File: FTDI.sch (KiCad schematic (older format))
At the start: 4 parts, among them U2 FT232RL

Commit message: ready for check by another person
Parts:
- U2: footprint Button_Switch_SMD:SW_SPST_B3S-1000 -> Package_SO:SSOP-28_5.3x10.2mm_P0.65mm
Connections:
- net 3V3VOUT renamed 3V3VDD
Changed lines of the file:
@@
 AR Path="/5E190CFD" Ref="C?"  Part="1"
 AR Path="/5E18BB0B/5E190CFD" Ref="C12"  Part="1"
-AR Path="/5EBF9349/5E190CFD" Ref="C?"  Part="1"
-F 0 "C?" V 5900 1900 50  0000 L CNN
+AR Path="/5EBF9349/5E190CFD" Ref="C34"  Part="1"
+F 0 "C34" V 5900 1900 50  0000 L CNN
 F 1 "0.1uF" V 6000 1850 50  0000 L CNN
 F 2 "Capacitor_SMD:C_0603_1608Metric" H 6188 1800 50  0001 C CNN
@@
 AR Path="/5E190D03" Ref="U?"  Part="1"
 AR Path="/5E18BB0B/5E190D03" Ref="U2"  Part="1"
-AR Path="/5EBF9349/5E190D03" Ref="U?"  Part="1"
-F 0 "U?" H 5100 4381 50  0000 C CNN
+AR Path="/5EBF9349/5E190D03" Ref="U2"  Part="1"
+F 0 "U2" H 5100 4381 50  0000 C CNN
 F 1 "FT232RL" H 5100 4290 50  0000 C CNN
-F 2 "Button_Switch_SMD:SW_SPST_B3S-1000" H 6200 2300 50  0001 C CNN
+F 2 "Package_SO:SSOP-28_5.3x10.2mm_P0.65mm" H 6200 2300 50  0001 C CNN
 F 3 "https://www.ftdichip.com/Support/Documents/DataSheets/ICs/DS_FT232R.pdf" H 5100 3200 50  0001 C CNN
 	1    5100 3200
@@
 AR Path="/5E190D1F" Ref="C?"  Part="1"
 AR Path="/5E18BB0B/5E190D1F" Ref="C1"  Part="1"
-AR Path="/5EBF9349/5E190D1F" Ref="C?"  Part="1"
-F 0 "C?" V 3800 1900 50  0000 L CNN
+AR Path="/5EBF9349/5E190D1F" Ref="C32"  Part="1"
+F 0 "C32" V 3800 1900 50  0000 L CNN
 F 1 "0.1uF" V 3900 1850 50  0000 L CNN
 F 2 "Capacitor_SMD:C_0603_1608Metric" H 4088 1800 50  0001 C CNN
@@
 AR Path="/5E190D4F" Ref="C?"  Part="1"
 AR Path="/5E18BB0B/5E190D4F" Ref="C2"  Part="1"
-AR Path="/5EBF9349/5E190D4F" Ref="C?"  Part="1"
-F 0 "C?" V 4300 2450 50  0000 L CNN
+AR Path="/5EBF9349/5E190D4F" Ref="C33"  Part="1"
+F 0 "C33" V 4300 2450 50  0000 L CNN
 F 1 "0.1uF" V 4200 2400 50  0000 L CNN
 F 2 "Capacitor_SMD:C_0603_1608Metric" H 4088 2350 50  0001 C CNN
@@
 Text HLabel 3800 4400 3    50   Input ~ 0
 DGND
+Text HLabel 4850 1750 0    50   BiDi ~ 0
+3V3VDD
 $EndSCHEMATC

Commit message: updating sib-kicad-footprint commit
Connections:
- net 3V3VDD: no longer names the net of C1.1, C2.2, U2.17 (3V3OUT), U2.4 (VCCIO)
- net 3V3VDD: no longer U2.19 (~RESET~)
- new net 3V3VOUT: U2.19 (~RESET~)
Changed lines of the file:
@@
 EESchema Schematic File Version 4
 LIBS:aducm_board-cache
-EELAYER 26 0
+EELAYER 30 0
 EELAYER END
 $Descr A4 11693 8268
@@
 	5900 2600 6250 2600
 Wire Wire Line
-	4850 1750 5000 1750
-Wire Wire Line
-	5000 1750 5000 1950
-Wire Wire Line
 	5350 1750 5200 1750
 Wire Wire Line
 	5200 1750 5200 1950
-Connection ~ 5000 1950
 Connection ~ 5200 1950
 Wire Wire Line
@@
 Text HLabel 6250 2600 2    50   Input ~ 0
 SOUT
-Text Label 4850 1750 0    50   ~ 0
-3V3VOUT
 Text Label 3850 3200 0    50   ~ 0
 3V3VOUT
@@
 Text HLabel 3800 4400 3    50   Input ~ 0
 DGND
-Text HLabel 4850 1750 0    50   BiDi ~ 0
-3V3VDD
 $EndSCHEMATC

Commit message: schematic and pcb redesign
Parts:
- C39: renamed from C1; footprint Capacitor_SMD:C_0603_1608Metric -> Capacitor_SMD:C_0402_1005Metric
- C40: renamed from C2; footprint Capacitor_SMD:C_0603_1608Metric -> Capacitor_SMD:C_0402_1005Metric
- C41: renamed from C12; footprint Capacitor_SMD:C_0603_1608Metric -> Capacitor_SMD:C_0402_1005Metric
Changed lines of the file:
@@
 EESchema Schematic File Version 4
-LIBS:aducm_board-cache
 EELAYER 30 0
 EELAYER END
 $Descr A4 11693 8268
 encoding utf-8
-Sheet 4 5
+Sheet 3 5
 Title "ADuCM355 Template"
 Date ""
@@
 P 6150 1950
 AR Path="/5E190CFD" Ref="C?"  Part="1"
-AR Path="/5E18BB0B/5E190CFD" Ref="C12"  Part="1"
-AR Path="/5EBF9349/5E190CFD" Ref="C34"  Part="1"
-F 0 "C34" V 5900 1900 50  0000 L CNN
+AR Path="/5E18BB0B/5E190CFD" Ref="C?"  Part="1"
+AR Path="/5EBF9349/5E190CFD" Ref="C41"  Part="1"
+F 0 "C41" V 5900 1900 50  0000 L CNN
 F 1 "0.1uF" V 6000 1850 50  0000 L CNN
-F 2 "Capacitor_SMD:C_0603_1608Metric" H 6188 1800 50  0001 C CNN
+F 2 "Capacitor_SMD:C_0402_1005Metric" H 6188 1800 50  0001 C CNN
 F 3 "~" H 6150 1950 50  0001 C CNN
 	1    6150 1950
@@
 P 5100 3200
 AR Path="/5E190D03" Ref="U?"  Part="1"
-AR Path="/5E18BB0B/5E190D03" Ref="U2"  Part="1"
+AR Path="/5E18BB0B/5E190D03" Ref="U?"  Part="1"
 AR Path="/5EBF9349/5E190D03" Ref="U2"  Part="1"
 F 0 "U2" H 5100 4381 50  0000 C CNN
@@
 P 4050 1950
 AR Path="/5E190D1F" Ref="C?"  Part="1"
-AR Path="/5E18BB0B/5E190D1F" Ref="C1"  Part="1"
-AR Path="/5EBF9349/5E190D1F" Ref="C32"  Part="1"
-F 0 "C32" V 3800 1900 50  0000 L CNN
+AR Path="/5E18BB0B/5E190D1F" Ref="C?"  Part="1"
+AR Path="/5EBF9349/5E190D1F" Ref="C39"  Part="1"
+F 0 "C39" V 3800 1900 50  0000 L CNN
 F 1 "0.1uF" V 3900 1850 50  0000 L CNN
-F 2 "Capacitor_SMD:C_0603_1608Metric" H 4088 1800 50  0001 C CNN
+F 2 "Capacitor_SMD:C_0402_1005Metric" H 4088 1800 50  0001 C CNN
 F 3 "~" H 4050 1950 50  0001 C CNN
 	1    4050 1950
@@
 P 4050 2500
 AR Path="/5E190D4F" Ref="C?"  Part="1"
-AR Path="/5E18BB0B/5E190D4F" Ref="C2"  Part="1"
-AR Path="/5EBF9349/5E190D4F" Ref="C33"  Part="1"
-F 0 "C33" V 4300 2450 50  0000 L CNN
+AR Path="/5E18BB0B/5E190D4F" Ref="C?"  Part="1"
+AR Path="/5EBF9349/5E190D4F" Ref="C40"  Part="1"
+F 0 "C40" V 4300 2450 50  0000 L CNN
 F 1 "0.1uF" V 4200 2400 50  0000 L CNN
-F 2 "Capacitor_SMD:C_0603_1608Metric" H 4088 2350 50  0001 C CNN
+F 2 "Capacitor_SMD:C_0402_1005Metric" H 4088 2350 50  0001 C CNN
 F 3 "~" H 4050 2500 50  0001 C CNN
 	1    4050 2500

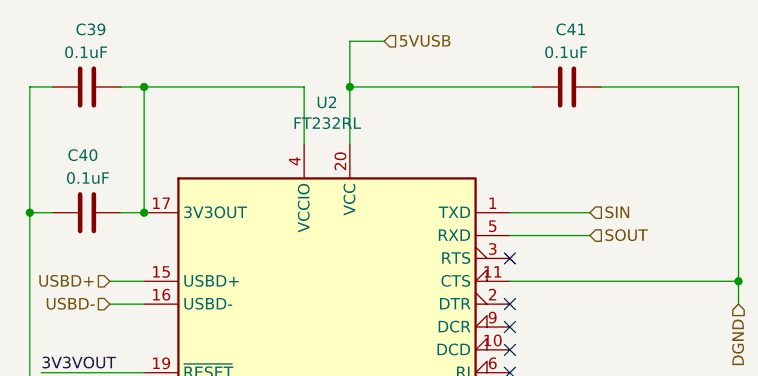
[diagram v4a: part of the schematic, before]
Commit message: finsihed traces for one EC sensor
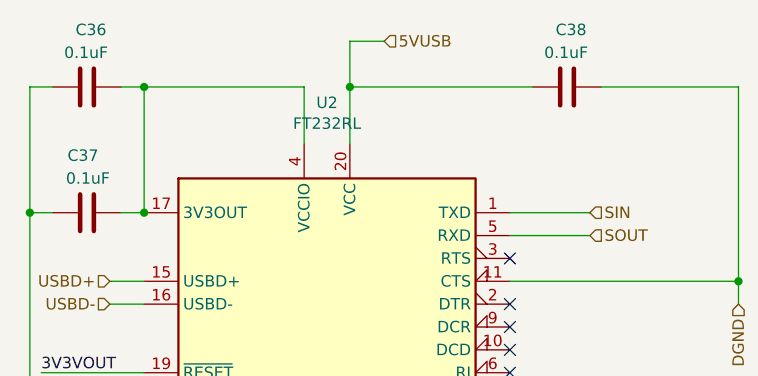
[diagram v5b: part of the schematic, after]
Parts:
- renumbered C39 to C36, C40 to C37, C41 to C38
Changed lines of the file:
@@
 AR Path="/5E190CFD" Ref="C?"  Part="1"
 AR Path="/5E18BB0B/5E190CFD" Ref="C?"  Part="1"
-AR Path="/5EBF9349/5E190CFD" Ref="C41"  Part="1"
-F 0 "C41" V 5900 1900 50  0000 L CNN
+AR Path="/5EBF9349/5E190CFD" Ref="C38"  Part="1"
+F 0 "C38" V 5900 1900 50  0000 L CNN
 F 1 "0.1uF" V 6000 1850 50  0000 L CNN
 F 2 "Capacitor_SMD:C_0402_1005Metric" H 6188 1800 50  0001 C CNN
@@
 AR Path="/5E190D1F" Ref="C?"  Part="1"
 AR Path="/5E18BB0B/5E190D1F" Ref="C?"  Part="1"
-AR Path="/5EBF9349/5E190D1F" Ref="C39"  Part="1"
-F 0 "C39" V 3800 1900 50  0000 L CNN
+AR Path="/5EBF9349/5E190D1F" Ref="C36"  Part="1"
+F 0 "C36" V 3800 1900 50  0000 L CNN
 F 1 "0.1uF" V 3900 1850 50  0000 L CNN
 F 2 "Capacitor_SMD:C_0402_1005Metric" H 4088 1800 50  0001 C CNN
@@
 AR Path="/5E190D4F" Ref="C?"  Part="1"
 AR Path="/5E18BB0B/5E190D4F" Ref="C?"  Part="1"
-AR Path="/5EBF9349/5E190D4F" Ref="C40"  Part="1"
-F 0 "C40" V 4300 2450 50  0000 L CNN
+AR Path="/5EBF9349/5E190D4F" Ref="C37"  Part="1"
+F 0 "C37" V 4300 2450 50  0000 L CNN
 F 1 "0.1uF" V 4200 2400 50  0000 L CNN
 F 2 "Capacitor_SMD:C_0402_1005Metric" H 4088 2350 50  0001 C CNN

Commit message: first draft done, needs reviewing
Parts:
- removed U2: FT232RL, Package_SO:SSOP-28_5.3x10.2mm_P0.65mm, symbol Interface_USB:FT232RL
- added U2: FT232RQ, Package_DFN_QFN:QFN-32-1EP_5x5mm_P0.5mm_EP3.3x3.3mm, symbol SIB_Footprint:FT232RQ
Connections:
- net 3V3VOUT: now also C36.1, C37.2, U2.1 (VCCIO), U2.16 (3V3OUT), U2.18 (RESET#)
- net 5VUSB: now also U2.19 (VCC)
- net DGND: now also U2.17 (GND), U2.20 (GND), U2.24 (AGND), U2.26 (TEST), U2.33 (PAD), U2.4 (GND), U2.8 (CTS#)
- net SIN: now also U2.30 (TXD)
- net SOUT: now also U2.2 (RXD)
- net USBD+: now also U2.14 (USBDP)
- net USBD-: now also U2.15 (USBDM)
- no-connect marks 12 -> 18
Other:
- note removed: "FTDI USB to UART"
- moved on the sheet: C36, C37, C38
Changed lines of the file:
@@
 L Device:C C?
 U 1 1 5E190CFD
-P 6150 1950
+P 4500 2200
 AR Path="/5E190CFD" Ref="C?"  Part="1"
 AR Path="/5E18BB0B/5E190CFD" Ref="C?"  Part="1"
 AR Path="/5EBF9349/5E190CFD" Ref="C38"  Part="1"
-F 0 "C38" V 5900 1900 50  0000 L CNN
-F 1 "0.1uF" V 6000 1850 50  0000 L CNN
-F 2 "Capacitor_SMD:C_0402_1005Metric" H 6188 1800 50  0001 C CNN
-F 3 "~" H 6150 1950 50  0001 C CNN
-	1    6150 1950
-	0    1    1    0
+F 0 "C38" V 4250 2150 50  0000 L CNN
+F 1 "0.1uF" V 4350 2100 50  0000 L CNN
+F 2 "Capacitor_SMD:C_0402_1005Metric" H 4538 2050 50  0001 C CNN
+F 3 "~" H 4500 2200 50  0001 C CNN
+	1    4500 2200
+	-1   0    0    1
 $EndComp
-$Comp
-L Interface_USB:FT232RL U?
-U 1 1 5E190D03
-P 5100 3200
-AR Path="/5E190D03" Ref="U?"  Part="1"
-AR Path="/5E18BB0B/5E190D03" Ref="U?"  Part="1"
-AR Path="/5EBF9349/5E190D03" Ref="U2"  Part="1"
-F 0 "U2" H 5100 4381 50  0000 C CNN
-F 1 "FT232RL" H 5100 4290 50  0000 C CNN
-F 2 "Package_SO:SSOP-28_5.3x10.2mm_P0.65mm" H 6200 2300 50  0001 C CNN
-F 3 "https://www.ftdichip.com/Support/Documents/DataSheets/ICs/DS_FT232R.pdf" H 5100 3200 50  0001 C CNN
-	1    5100 3200
-	1    0    0    -1
-$EndComp
-Wire Wire Line
-	4900 4200 4900 4300
-Wire Wire Line
-	4900 4300 5100 4300
-Wire Wire Line
-	5100 4300 5100 4200
-Connection ~ 4900 4300
-Wire Wire Line
-	4900 4300 4900 4450
-Wire Wire Line
-	5100 4300 5200 4300
-Wire Wire Line
-	5200 4300 5200 4200
-Connection ~ 5100 4300
-Wire Wire Line
-	5200 4300 5300 4300
-Wire Wire Line
-	5300 4300 5300 4200
-Connection ~ 5200 4300
-NoConn ~ 4300 3400
-NoConn ~ 4300 3600
-Wire Wire Line
-	4300 3900 3800 3900
-Connection ~ 3800 3900
-Wire Wire Line
-	3800 3900 3800 4400
-Wire Wire Line
-	4300 3200 3850 3200
 $Comp
 L Device:C C?
 U 1 1 5E190D1F
-P 4050 1950
+P 4250 2900
 AR Path="/5E190D1F" Ref="C?"  Part="1"
 AR Path="/5E18BB0B/5E190D1F" Ref="C?"  Part="1"
 AR Path="/5EBF9349/5E190D1F" Ref="C36"  Part="1"
-F 0 "C36" V 3800 1900 50  0000 L CNN
-F 1 "0.1uF" V 3900 1850 50  0000 L CNN
-F 2 "Capacitor_SMD:C_0402_1005Metric" H 4088 1800 50  0001 C CNN
-F 3 "~" H 4050 1950 50  0001 C CNN
-	1    4050 1950
-	0    1    1    0
+F 0 "C36" V 4000 2850 50  0000 L CNN
+F 1 "0.1uF" V 4100 2800 50  0000 L CNN
+F 2 "Capacitor_SMD:C_0402_1005Metric" H 4288 2750 50  0001 C CNN
+F 3 "~" H 4250 2900 50  0001 C CNN
+	1    4250 2900
+	1    0    0    -1
 $EndComp
-NoConn ~ 5900 3500
-NoConn ~ 5900 3600
-NoConn ~ 5900 3700
-NoConn ~ 5900 3800
-NoConn ~ 5900 3900
-NoConn ~ 5900 2700
-NoConn ~ 5900 2900
-NoConn ~ 5900 3000
-NoConn ~ 5900 3100
-NoConn ~ 5900 3200
-Wire Wire Line
-	6250 2500 5900 2500
-Wire Wire Line
-	5900 2600 6250 2600
-Wire Wire Line
-	5350 1750 5200 1750
-Wire Wire Line
-	5200 1750 5200 1950
-Connection ~ 5200 1950
-Wire Wire Line
-	5200 1950 5200 2200
-Wire Wire Line
-	5000 1950 5000 2200
-Wire Wire Line
-	6900 1950 6900 2800
-Connection ~ 6900 2800
-Wire Wire Line
-	6900 2800 6900 2900
-Wire Wire Line
-	5900 2800 6900 2800
-Text Notes 5400 4600 0    50   ~ 0
-FTDI USB to UART
 $Comp
 L Device:C C?
 U 1 1 5E190D4F
-P 4050 2500
+P 4250 4850
 AR Path="/5E190D4F" Ref="C?"  Part="1"
 AR Path="/5E18BB0B/5E190D4F" Ref="C?"  Part="1"
 AR Path="/5EBF9349/5E190D4F" Ref="C37"  Part="1"
-F 0 "C37" V 4300 2450 50  0000 L CNN
-F 1 "0.1uF" V 4200 2400 50  0000 L CNN
-F 2 "Capacitor_SMD:C_0402_1005Metric" H 4088 2350 50  0001 C CNN
-F 3 "~" H 4050 2500 50  0001 C CNN
-	1    4050 2500
-	0    -1   -1   0
+F 0 "C37" V 4500 4800 50  0000 L CNN
+F 1 "0.1uF" V 4400 4750 50  0000 L CNN
+F 2 "Capacitor_SMD:C_0402_1005Metric" H 4288 4700 50  0001 C CNN
+F 3 "~" H 4250 4850 50  0001 C CNN
+	1    4250 4850
+	-1   0    0    1
 $EndComp
+$Comp
+L SIB_Footprint:FT232RQ U2
+U 1 1 601E1423
+P 5800 3650
+F 0 "U2" H 5800 4965 50  0000 C CNN
+F 1 "FT232RQ" H 5800 4874 50  0000 C CNN
+F 2 "Package_DFN_QFN:QFN-32-1EP_5x5mm_P0.5mm_EP3.3x3.3mm" H 5800 3650 50  0001 C CNN
+F 3 "" H 5800 3650 50  0001 C CNN
+	1    5800 3650
+	1    0    0    -1
+$EndComp
+Text HLabel 6650 2750 2    50   Input ~ 0
+SIN
+Text HLabel 6650 2900 2    50   Input ~ 0
+SOUT
 Wire Wire Line
-	4150 2900 4300 2900
+	6500 2750 6650 2750
 Wire Wire Line
-	4150 2800 4300 2800
+	6500 2900 6650 2900
+Text HLabel 6650 3200 2    50   Input ~ 0
+DGND
 Wire Wire Line
-	4300 1950 5000 1950
+	6650 3200 6500 3200
+NoConn ~ 6650 3050
 Wire Wire Line
-	4300 2500 4300 1950
-Connection ~ 4300 1950
+	6500 3050 6650 3050
+NoConn ~ 6650 3350
+NoConn ~ 6650 3500
+NoConn ~ 6650 3650
+NoConn ~ 6650 3800
+NoConn ~ 6650 3950
+NoConn ~ 6650 4100
+NoConn ~ 6650 4250
+NoConn ~ 6650 4400
+NoConn ~ 6650 4550
 Wire Wire Line
-	4200 1950 4300 1950
+	6650 3350 6500 3350
 Wire Wire Line
-	3900 1950 3800 1950
+	6650 3500 6500 3500
 Wire Wire Line
-	4200 2500 4300 2500
-Connection ~ 4300 2500
+	6650 3650 6500 3650
 Wire Wire Line
-	3800 1950 3800 2500
+	6650 3800 6500 3800
 Wire Wire Line
-	3900 2500 3800 2500
-Connection ~ 3800 2500
+	6650 3950 6500 3950
 Wire Wire Line
-	3800 2500 3800 3900
+	6500 4100 6650 4100
 Wire Wire Line
-	5200 1950 6000 1950
+	6650 4250 6500 4250
 Wire Wire Line
-	6300 1950 6900 1950
-Text HLabel 4150 2800 0    50   Input ~ 0
+	6650 4400 6500 4400
+Wire Wire Line
+	6650 4550 6500 4550
+NoConn ~ 4950 3350
+NoConn ~ 4950 3500
+NoConn ~ 4950 3650
+NoConn ~ 4950 3800
+NoConn ~ 4950 3950
+NoConn ~ 4950 4250
+NoConn ~ 4950 4400
+NoConn ~ 4950 4550
+Wire Wire Line
+	4950 3350 5100 3350
+Wire Wire Line
+	4950 3500 5100 3500
+Wire Wire Line
+	4950 3650 5100 3650
+Wire Wire Line
+	4950 3800 5100 3800
+Wire Wire Line
+	4950 3950 5100 3950
+Wire Wire Line
+	4950 4250 5100 4250
+Wire Wire Line
+	4950 4400 5100 4400
+Wire Wire Line
+	4950 4550 5100 4550
+Text Label 4950 4100 2    50   ~ 0
+3V3VOUT
+Wire Wire Line
+	5100 4100 4950 4100
+Text HLabel 4950 3200 0    50   Input ~ 0
 USBD+
-Text HLabel 4150 2900 0    50   Input ~ 0
+Text HLabel 4950 3050 0    50   Input ~ 0
 USBD-
-Text HLabel 6250 2500 2    50   Input ~ 0
-SIN
-Text HLabel 6250 2600 2    50   Input ~ 0
-SOUT
-Text Label 3850 3200 0    50   ~ 0
+Wire Wire Line
+	4950 3050 5100 3050
+Wire Wire Line
+	4950 3200 5100 3200
+Wire Wire Line
+	5100 2750 4450 2750
+Wire Wire Line
+	4450 2750 4450 4700
+Wire Wire Line
+	4450 4700 5100 4700
+Wire Wire Line
+	4250 4700 4450 4700
+Connection ~ 4450 4700
+Wire Wire Line
+	4450 2750 4250 2750
+Connection ~ 4450 2750
+Text HLabel 4250 5000 3    50   Input ~ 0
+DGND
+Text HLabel 4250 3050 3    50   Input ~ 0
+DGND
+Text HLabel 5650 5100 3    50   Input ~ 0
+DGND
+Wire Wire Line
+	5650 4950 5650 5000
+Wire Wire Line
+	5650 5000 5750 5000
+Wire Wire Line
+	5750 5000 5750 4950
+Connection ~ 5650 5000
+Wire Wire Line
+	5650 5000 5650 5100
+Wire Wire Line
+	5750 5000 5850 5000
+Wire Wire Line
+	5850 5000 5850 4950
+Connection ~ 5750 5000
+Wire Wire Line
+	5850 5000 5950 5000
+Wire Wire Line
+	5950 5000 5950 4950
+Connection ~ 5850 5000
+Wire Wire Line
+	5950 4950 6050 4950
+Wire Wire Line
+	6050 4950 6050 5000
+Wire Wire Line
+	6050 5000 5950 5000
+Connection ~ 5950 5000
+Text HLabel 4950 2900 0    50   Input ~ 0
+5VUSB
+Wire Wire Line
+	4950 2900 5100 2900
+Text HLabel 4250 2050 0    50   Input ~ 0
+5VUSB
+Text HLabel 4500 2350 3    50   Input ~ 0
+DGND
+Wire Wire Line
+	4250 2050 4500 2050
+Text Label 4600 4700 3    50   ~ 0
 3V3VOUT
-Text HLabel 5350 1750 2    50   Input ~ 0
-5VUSB
-Text HLabel 6900 2900 3    50   Input ~ 0
-DGND
-Text HLabel 4900 4450 3    50   Input ~ 0
-DGND
-Text HLabel 3800 4400 3    50   Input ~ 0
-DGND
+Wire Wire Line
+	6150 4950 6150 5000
+Wire Wire Line
+	6150 5000 6050 5000
+Connection ~ 6050 5000
 $EndSCHEMATC
